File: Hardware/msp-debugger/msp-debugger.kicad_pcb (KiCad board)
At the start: 2 copper layers, 127 x 82.5 mm, 23 parts, among them J1 USB_B_Micro, J2 Conn_02x10, U1 ESP32-S2-SOLO, U2 NHD-0420H1Z, U3 BA033CC0FP-E2

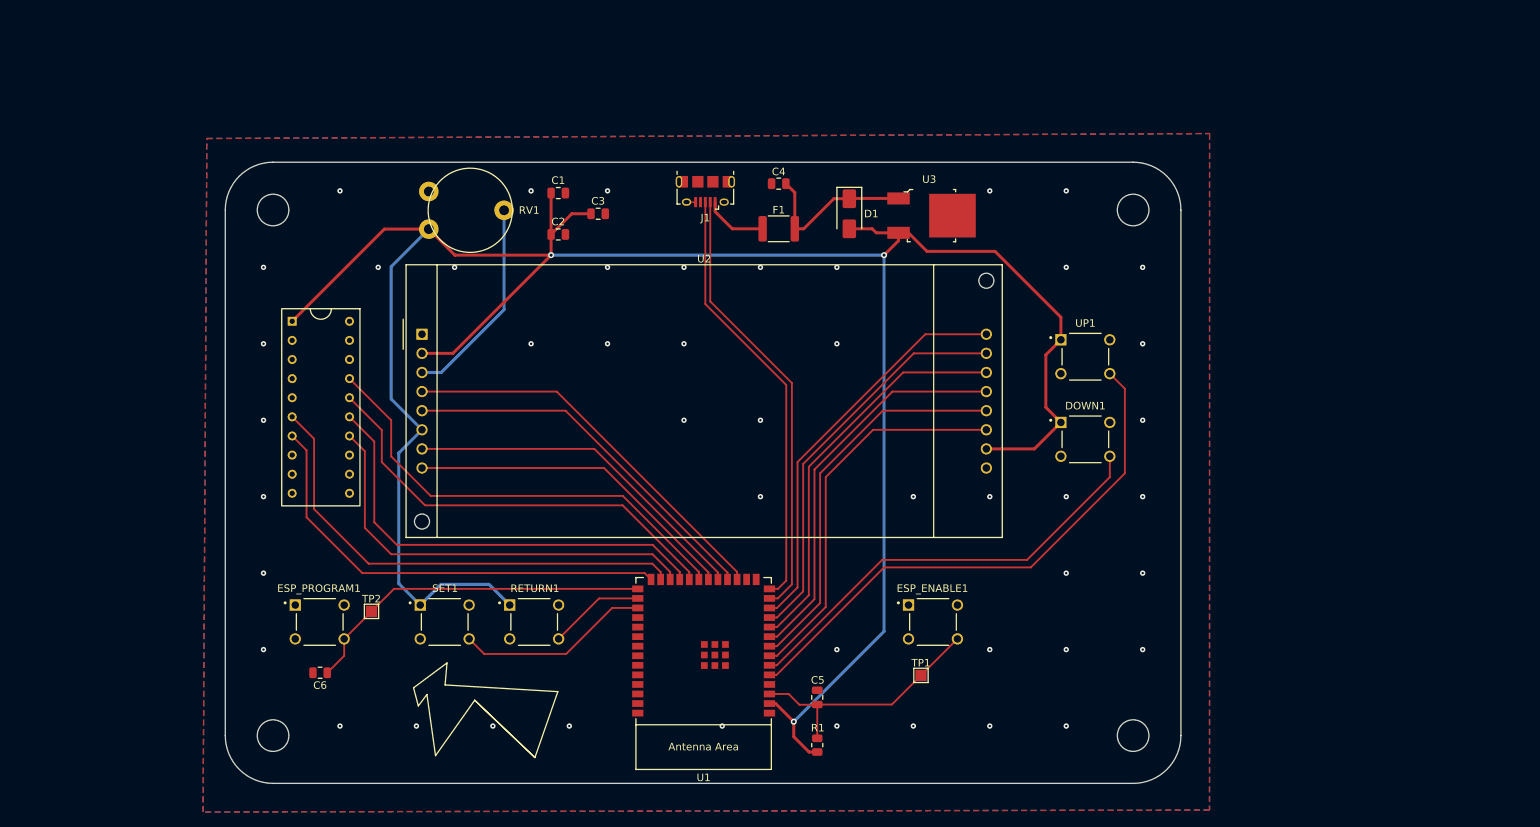
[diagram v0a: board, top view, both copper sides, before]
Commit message: begin updating pcb with g2553
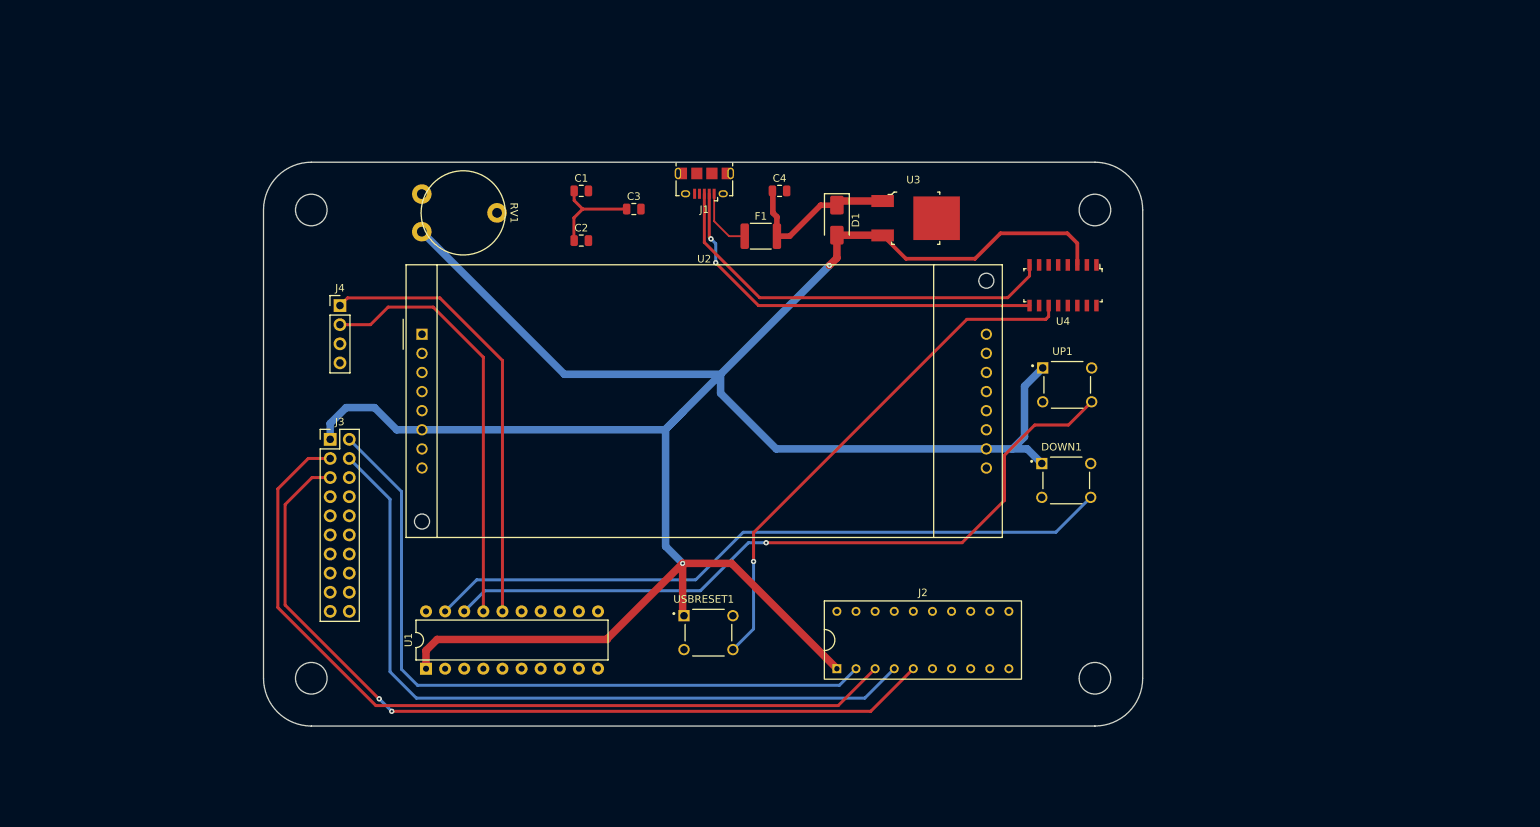
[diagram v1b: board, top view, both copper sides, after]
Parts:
- removed C5, C6: 0.1uF, Capacitor_SMD:C_0805_2012Metric
- removed ESP_ENABLE1, ESP_PROGRAM1, RETURN1, SET1: 222ADVBA, buttons:SW_222ADVBA
- removed R1: 10k, Resistor_SMD:R_0805_2012Metric
- removed TP1, TP2: TestPoint, TestPoint:TestPoint_Pad_1.5x1.5mm
- added J3: Conn_02x10, Connector_PinHeader_2.54mm:PinHeader_2x10_P2.54mm_Vertical, F.Cu at (90.1, 94.0)
- added J4: Conn_01x04_Pin, Connector_PinHeader_2.54mm:PinHeader_1x04_P2.54mm_Vertical, F.Cu at (91.4, 76.2)
- added U4: FT230XS-R, digikey-footprints:SOIC-16_W3.90mm, F.Cu at (187.5, 73.5)
- added USBRESET1: 222ADVBA, buttons:SW_222ADVBA, F.Cu at (140.4, 119.7)
- U1: value ESP32-S2-SOLO -> MSP430G2553IN20; footprint Espressif:ESP32-S2-SOLO -> Package_DIP:DIP-20_W7.62mm
- moved J2 85.8 mm to (168.9, 120.7), turned to 0 degrees
- moved U1 37.0 mm to (102.9, 124.5), turned to 90 degrees
- moved DOWN1 6.02 mm to (188.0, 99.4)
- moved C3 4.78 mm to (130.5, 63.4)
- moved UP1 4.45 mm to (188.1, 86.7)
- moved C2 3.17 mm to (123.5, 67.6)
- moved C1 3.07 mm to (123.5, 61.0)
- moved F1 2.57 mm to (147.4, 67.0)
- moved U3 2.14 mm to (167.6, 64.6)
- moved D1 1.86 mm to (157.5, 64.8)
- moved J1 1.12 mm to (139.9, 59.9)
- moved RV1 1.00 mm to (107.3, 63.9)
- moved C4 0.97 mm to (149.9, 61.0), turned to 0 degrees
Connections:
- J2 pad 10: unconnected-(J2-Pin_10-Pad10) -> /P10
- J2 pad 11: unconnected-(J2-Pin_11-Pad11) -> /P11
- J2 pad 12: unconnected-(J2-Pin_12-Pad12) -> /P12
- J2 pad 13: unconnected-(J2-Pin_13-Pad13) -> /P13
- J2 pad 18: unconnected-(J2-Pin_18-Pad18) -> /P18
- J2 pad 19: unconnected-(J2-Pin_19-Pad19) -> /P19
- J2 pad 2: unconnected-(J2-Pin_2-Pad2) -> /P2
- J2 pad 3: unconnected-(J2-Pin_3-Pad3) -> /P3
- J2 pad 4: unconnected-(J2-Pin_4-Pad4) -> /P4
- J2 pad 5: unconnected-(J2-Pin_5-Pad5) -> /P5
- J2 pad 8: unconnected-(J2-Pin_8-Pad8) -> /P8
- J2 pad 9: unconnected-(J2-Pin_9-Pad9) -> /P9
- U1 pad 1: GND -> +3.3V
- U1 pad 10: /DB4 -> /TMS
- U1 pad 11: /DB3 -> /TDO
- U1 pad 12: /DB2 -> /RST
- U1 pad 13: /D- -> /TEST
- U1 pad 14: /D+ -> /DB5
- U1 pad 15: unconnected-(U1-GPIO3/TOUCH3/ADC1_CH2-Pad15) -> /DB4
- U1 pad 16: unconnected-(U1-GPIO46-Pad16) -> /SBWTDIO
- U1 pad 17: /LCD RS -> /SBWTCK
- U1 pad 18: /LCD R/W -> /UP SW
- U1 pad 19: /DB0 -> /DOWN SW
- U1 pad 2: +3.3V -> /LCD R/W
- U1 pad 20: /DB1 -> GND
- U1 pad 3: /ESP EN -> /BC_RX
- U1 pad 4: unconnected-(U1-GPIO4/TOUCH4/ADC1_CH3-Pad4) -> /BC_TX
- U1 pad 5: /UP SW -> /LCD RS
- U1 pad 6: /DOWN SW -> /DB7
- U1 pad 7: /DB7 -> /DB6
- U1 pad 8: /DB6 -> /TDI
- U1 pad 9: /DB5 -> /TCK
- U2 pad 10: /DB3 -> unconnected-(U2-DB3-Pad10)
- U2 pad 7: /DB0 -> unconnected-(U2-DB0-Pad7)
- U2 pad 8: /DB1 -> unconnected-(U2-DB1-Pad8)
- U2 pad 9: /DB2 -> unconnected-(U2-DB2-Pad9)
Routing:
- net /P5: track 0.00 -> 112.5 mm, vias 0 -> 2
- net /P3: track 0.00 -> 111.2 mm
- net /P4: track 0.00 -> 100.7 mm
- net /P2: track 0.00 -> 95.6 mm
- net Net-(U4-RESET#): track 0.00 -> 69.2 mm, vias 0 -> 1
- net /TCK: track 64.0 -> 0.00 mm
- net /TEST: track 60.9 -> 0.00 mm
- net /TMS: track 60.8 -> 0.00 mm
- net /TDO: track 59.7 -> 0.00 mm
- net /SBWTDIO: track 0.00 -> 58.8 mm
- net /RST: track 58.2 -> 0.00 mm
- net /TDI: track 57.1 -> 0.00 mm
- net /SBWTCK: track 0.00 -> 56.6 mm
- net /DB2: track 53.7 -> 0.00 mm
- net /DB3: track 53.3 -> 0.00 mm
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- removed copper zone on B.Cu, net GND
- removed copper zone on F.Cu, net GND
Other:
- board size 127 x 82.5 mm -> 116.8 x 74.9 mm

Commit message: route new pcb
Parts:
- moved U4 0.75 mm to (187.9, 74.2), turned to 0 degrees
- moved U2 0.07 mm to (102.4, 80.0)
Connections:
- C4 pad 1: Net-(D1-K) -> +5V
- D1 pad 1: Net-(D1-K) -> +5V
- F1 pad 2: Net-(D1-K) -> +5V
- U3 pad 1: Net-(D1-K) -> +5V
- U4 pad 12: Net-(U4-VCC) -> +5V
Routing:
- net /BC_TX: track 0.00 -> 168.8 mm, vias 0 -> 4
- net /BC_RX: track 0.00 -> 166.6 mm, vias 0 -> 4
- net /TDO: track 0.00 -> 120.1 mm, vias 0 -> 2
- net /TCK: track 0.00 -> 113.2 mm, vias 0 -> 2
- net /TMS: track 0.00 -> 109.4 mm, vias 0 -> 2
- net /TEST: track 0.00 -> 104.8 mm, vias 0 -> 1
- net /TDI: track 0.00 -> 103.2 mm, vias 0 -> 1
- net /P8: track 0.00 -> 101.8 mm, vias 0 -> 1
- net /P9: track 0.00 -> 99.8 mm, vias 0 -> 1
- net /P11: track 0.00 -> 95.9 mm
- net /P10: track 0.00 -> 95.8 mm
- net /P12: track 0.00 -> 94.6 mm
- net /P13: track 0.00 -> 93.2 mm
- net /RST: track 0.00 -> 89.9 mm, vias 0 -> 2
- net /DB4: track 0.00 -> 89.8 mm, vias 0 -> 2
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- added copper zone on B.Cu, net GND
- added copper zone on F.Cu, net GND

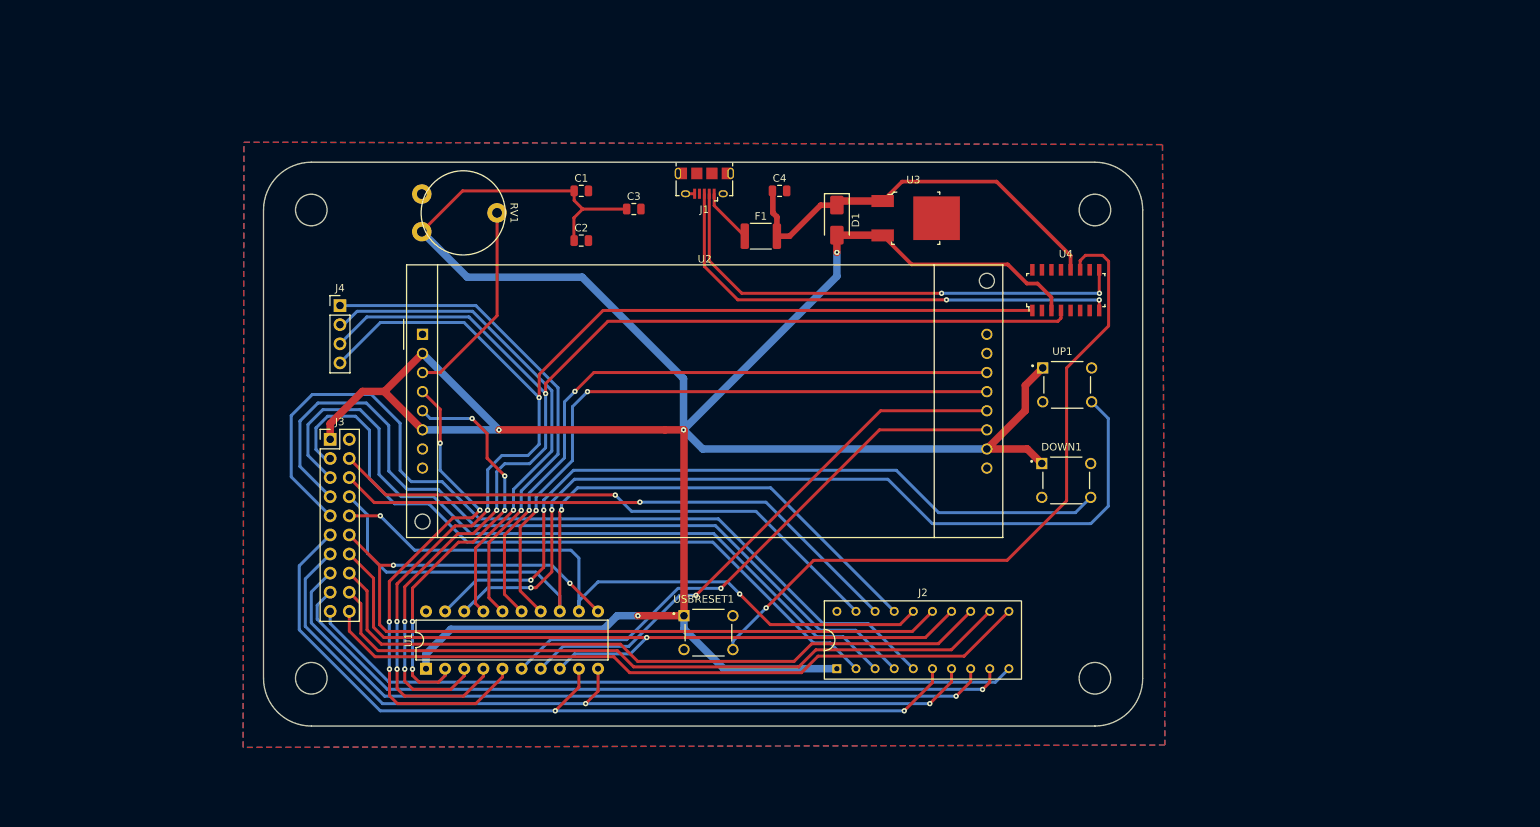
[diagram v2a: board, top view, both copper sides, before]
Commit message: reroute pcb for 40 line lcd screen
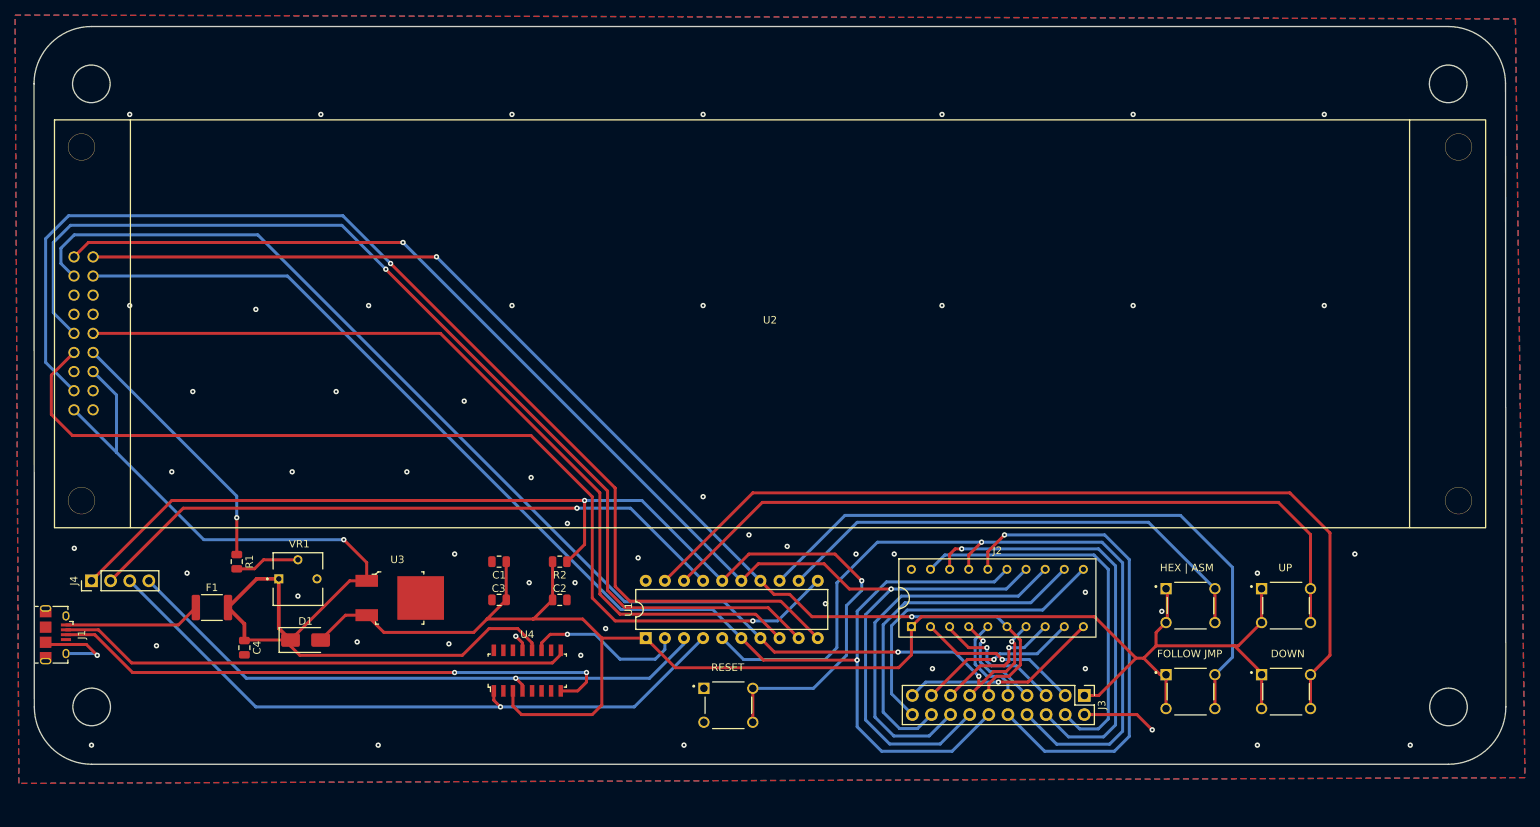
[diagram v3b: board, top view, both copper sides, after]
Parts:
- removed DOWN1, UP1, USBRESET1: 222ADVBA, buttons:SW_222ADVBA
- removed RV1: 10K-20K, project:Potentiometer_CTS_PTN10-E20HB20
- added R1: 10K, Capacitor_SMD:C_0805_2012Metric, F.Cu at (77.7, 110.2)
- added R2: 10K, Capacitor_SMD:C_0805_2012Metric, F.Cu at (120.7, 110.2)
- added SW1: 222ADVBA, buttons:SW_222ADVBA, F.Cu at (143.1, 129.3)
- added SW2: 222ADVBA, buttons:SW_222ADVBA, F.Cu at (204.5, 116.1)
- added SW3: 222ADVBA, buttons:SW_222ADVBA, F.Cu at (204.5, 127.5)
- added SW4: 222ADVBA, buttons:SW_222ADVBA, F.Cu at (217.2, 127.5)
- added SW5: 222ADVBA, buttons:SW_222ADVBA, F.Cu at (217.2, 116.1)
- added VR1: 10K, project:TRIM_3362P-1-103LF, F.Cu at (85.9, 112.5)
- C1: value 1uF -> 0.1uF
- C2: value 0.1uF -> 1uF
- U2: value NHD-0420H1Z -> ~; footprint Display:NHD-0420H1Z -> project:NHD-0440AZ-FL-YBW
- moved J3 105.8 mm to (190.4, 128.0), turned to -90 degrees
- moved J1 105.1 mm to (53.6, 119.9), turned to -90 degrees
- moved C4 93.5 mm to (78.7, 121.7), turned to -90 degrees
- moved D1 90.0 mm to (86.9, 120.7), turned to 0 degrees
- moved F1 88.1 mm to (74.4, 116.3)
- moved U4 87.6 mm to (116.3, 124.7)
- moved U3 85.1 mm to (99.1, 115.1)
- moved C3 54.9 mm to (112.6, 115.3), turned to 180 degrees
- moved C1 50.5 mm to (112.6, 110.2)
- moved J4 49.3 mm to (58.4, 112.8), turned to 90 degrees
- moved C2 47.8 mm to (120.7, 115.3)
- moved U2 46.2 mm to (148.6, 78.6)
- moved U1 29.5 mm to (132.1, 120.4)
- moved J2 11.4 mm to (178.8, 115.1)
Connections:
- net /SBWTDIO renamed /CNTL RST
- C1 pad 1: +3.3V -> GND
- C1 pad 2: GND -> +3.3V
- J2 pad 14: /TDI -> /DB7
- J2 pad 15: /TDO -> /DB4
- J2 pad 6: /TCK -> /DB6
- J2 pad 7: /TMS -> /DB5
- J3 pad 14: /TDI -> /DB7
- J3 pad 15: /TDO -> /DB4
- J3 pad 6: /TCK -> /DB6
- J3 pad 7: /TMS -> /DB5
- J4 pad 3: /BC_RX -> /BC_TX
- J4 pad 4: /BC_TX -> /BC_RX
- U1 pad 10: /TMS -> /E2
- U1 pad 11: /TDO -> /RS
- U1 pad 12: /RST -> /HEX SW
- U1 pad 13: /TEST -> /JMP SW
- U1 pad 14: /DB5 -> /DB6
- U1 pad 15: /DB4 -> /DB7
- U1 pad 2: /LCD R/W -> /RESET#
- U1 pad 5: /LCD RS -> /TEST
- U1 pad 6: /DB7 -> /DB4
- U1 pad 7: /DB6 -> /DB5
- U1 pad 8: /TDI -> /R/W
- U1 pad 9: /TCK -> /E1
- U2 pad 1: GND -> /DB7
- U2 pad 10: unconnected-(U2-DB3-Pad10) -> /R/W
- U2 pad 11: /DB4 -> /RS
- U2 pad 12: /DB5 -> Net-(U2-V_{0})
- U2 pad 13: /DB6 -> GND
- U2 pad 14: /DB7 -> +5V
- U2 pad 15: +3.3V -> /E2
- U2 pad 16: GND -> unconnected-(U2-NC-Pad16)
- U2 pad 2: +3.3V -> /DB6
- U2 pad 3: Net-(U2-VO) -> /DB5
- U2 pad 4: /LCD RS -> /DB4
- U2 pad 5: /LCD R/W -> unconnected-(U2-DB3-Pad5)
- U2 pad 6: +3.3V -> unconnected-(U2-DB2-Pad6)
- U2 pad 9: unconnected-(U2-DB2-Pad9) -> /E1
- U4 pad 11: Net-(U4-RESET#) -> /RESET#
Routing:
- net +3.3V: track 378.7 -> 221.0 mm, vias 4 -> 0
- net /E2: track 0.00 -> 156.6 mm, vias 0 -> 1
- net /E1: track 0.00 -> 143.7 mm, vias 0 -> 1
- net /RS: track 0.00 -> 132.8 mm, vias 0 -> 1
- net /TDO: track 120.1 -> 0.00 mm, vias 2 -> 0
- net /R/W: track 0.00 -> 115.9 mm
- net /TCK: track 113.2 -> 0.00 mm, vias 2 -> 0
- net /DB7: track 75.0 -> 184.9 mm, vias 1 -> 2
- net /TMS: track 109.4 -> 0.00 mm, vias 2 -> 0
- net /P5: track 118.1 -> 12.7 mm
- net /TDI: track 103.2 -> 0.00 mm, vias 1 -> 0
- net /P4: track 109.9 -> 13.7 mm, vias 0 -> 1
- net Net-(U4-RESET#): track 93.0 -> 0.00 mm, vias 1 -> 0
- net /DB4: track 89.8 -> 181.1 mm, vias 2 -> 1
- net /JMP SW: track 0.00 -> 86.4 mm
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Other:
- board size 116.8 x 74.9 mm -> 195.6 x 98 mm
